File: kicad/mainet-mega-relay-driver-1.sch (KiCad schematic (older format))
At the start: 8 parts, among them J30 Screw_Terminal_01x03, K1 SANYOU_SRD_Form_C, Q1 2N3904, U2 4N37

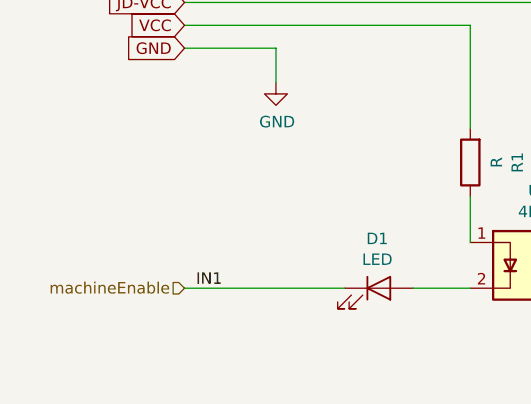
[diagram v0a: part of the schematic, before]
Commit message: Kicad: Modificaciones menores esquemáticos
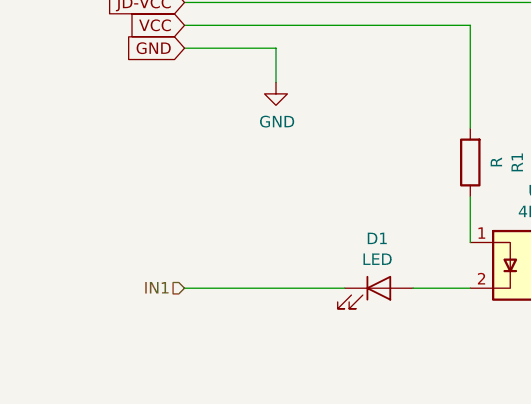
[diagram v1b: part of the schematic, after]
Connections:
- net machineEnable renamed IN1
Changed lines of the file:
@@
 $Descr A4 11693 8268
 encoding utf-8
-Sheet 6 17
+Sheet 8 17
 Title ""
 Date ""
@@
 Wire Wire Line
 	4450 4100 5150 4100
-Text HLabel 4450 4100 0    50   Input ~ 0
-machineEnable
 $Comp
 L power:GND #PWR?
@@
 Text GLabel 4450 3050 0    50   Input ~ 0
 GND
-Text Label 4500 4100 0    50   ~ 0
+Text HLabel 4450 4100 0    50   Input ~ 0
 IN1
 $EndSCHEMATC

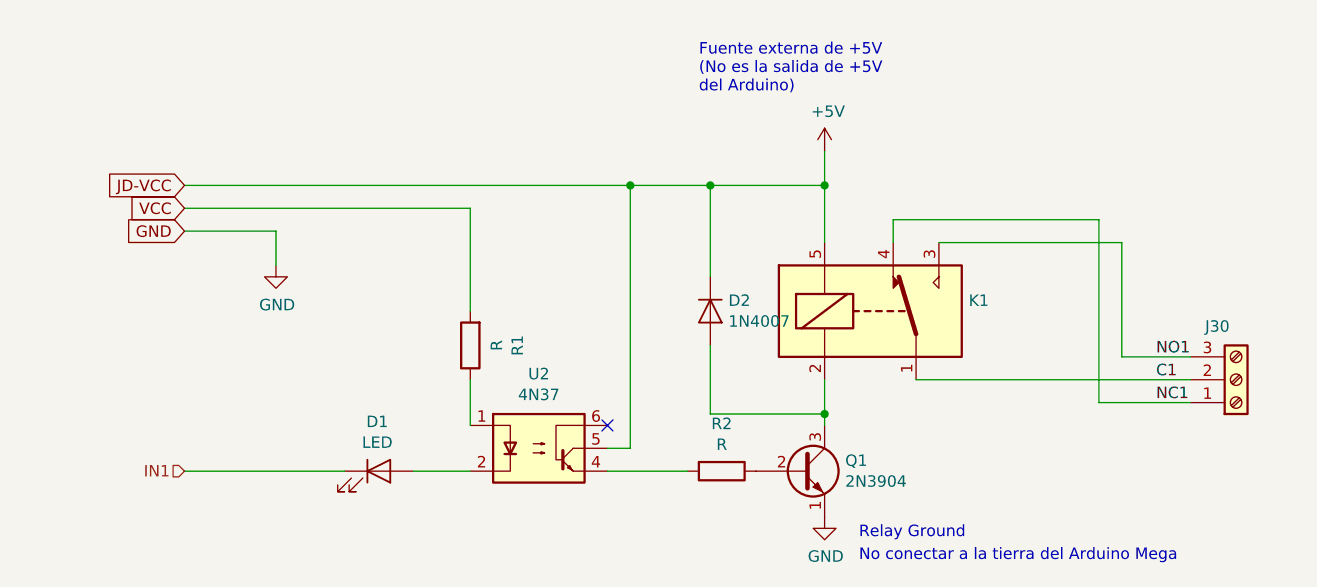
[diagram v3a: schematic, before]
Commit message: KICAD: Actualización de esquematicos del módulo de 8 relés de control
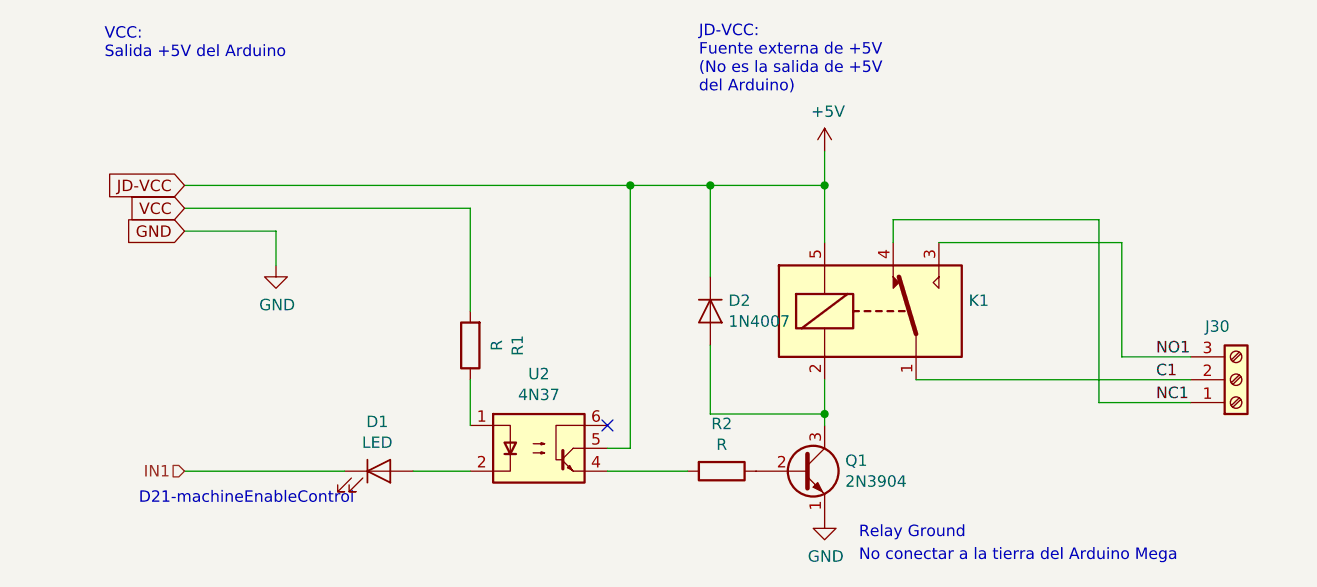
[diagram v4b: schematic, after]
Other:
- note added: "D21-machineEnableControl"
- note added: "JD-VCC:\nFuente externa de +5V\n(No es la salida de +5V \ndel Arduino)"
- note added: "VCC:\nSalida +5V del Arduino"
- note removed: "Fuente externa de +5V\n(No es la salida de +5V \ndel Arduino)"
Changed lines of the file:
@@
 EESchema Schematic File Version 4
 LIBS:mainet-mega-cache
-LIBS:mainet-mega-5V-to-mp-10v-cache
 EELAYER 30 0
 EELAYER END
 $Descr A4 11693 8268
 encoding utf-8
-Sheet 8 21
-Title ""
-Date ""
+Sheet 7 21
+Title "Relay driver 1"
+Date "2021-02-02"
 Rev ""
 Comp ""
@@
 $EndComp
 Text Notes 6700 2450 0    50   ~ 0
-Fuente externa de +5V\n(No es la salida de +5V \ndel Arduino)
+JD-VCC:\nFuente externa de +5V\n(No es la salida de +5V \ndel Arduino)
 Text Notes 7400 4400 0    50   ~ 0
 Relay Ground\n
@@
 Text HLabel 4450 4100 0    50   Input ~ 0
 IN1
+Text Notes 4250 4250 0    50   ~ 0
+D21-machineEnableControl
+Text Notes 4100 2300 0    50   ~ 0
+VCC:\nSalida +5V del Arduino
 $EndSCHEMATC
